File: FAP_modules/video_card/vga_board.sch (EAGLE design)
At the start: 32 parts, among them IC1 IS61LV256, IC2 IS61LV256

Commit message: vga pcb trace fix
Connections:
- net +3V3: now also LED2.A
- net GND: no longer R14.1
- net N$36: now also R14.1; no longer LED2.A
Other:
- moved on the sheet: LED2, R14
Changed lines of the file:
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@@
 <part name="LED2" library="cpu_board" deviceset="LED" device="CHIP-LED0805"/>
 <part name="R14" library="cpu_board" deviceset="RESISTOR" device="0805-RES"/>
-<part name="GND13" library="supply1" deviceset="GND" device=""/>
 <part name="JP1" library="pinhead" deviceset="PINHD-1X1" device=""/>
 <part name="JP2" library="pinhead" deviceset="PINHD-1X1" device=""/>
@@
 <part name="+3V10" library="supply1" deviceset="+3V3" device=""/>
 <part name="+3V11" library="supply1" deviceset="+3V3" device=""/>
+<part name="+3V12" library="supply1" deviceset="+3V3" device=""/>
 </parts>
 <sheets>
@@
 <instance part="GND12" gate="1" x="-566.42" y="-254"/>
 <instance part="+3V7" gate="G$1" x="-566.42" y="-231.14" rot="MR0"/>
-<instance part="LED2" gate="G$1" x="-274.32" y="-137.16"/>
-<instance part="R14" gate="G$1" x="-274.32" y="-147.32" rot="R90"/>
-<instance part="GND13" gate="1" x="-274.32" y="-154.94"/>
+<instance part="LED2" gate="G$1" x="-274.32" y="-114.3"/>
+<instance part="R14" gate="G$1" x="-274.32" y="-127" rot="R90"/>
 <instance part="JP1" gate="G$1" x="-256.54" y="-132.08"/>
 <instance part="JP2" gate="G$1" x="-231.14" y="-132.08"/>
@@
 <instance part="+3V10" gate="G$1" x="-520.7" y="193.04"/>
 <instance part="+3V11" gate="G$1" x="-510.54" y="193.04"/>
+<instance part="+3V12" gate="G$1" x="-274.32" y="-104.14"/>
 </instances>
 <busses>
@@
 </segment>
 <segment>
-<pinref part="R14" gate="G$1" pin="1"/>
-<pinref part="GND13" gate="1" pin="GND"/>
-</segment>
-<segment>
 <pinref part="JP2" gate="G$1" pin="1"/>
 <pinref part="GND14" gate="1" pin="GND"/>
@@
 <pinref part="+3V11" gate="G$1" pin="+3V3"/>
 </segment>
+<segment>
+<pinref part="+3V12" gate="G$1" pin="+3V3"/>
+<pinref part="LED2" gate="G$1" pin="A"/>
+<wire x1="-274.32" y1="-111.76" x2="-274.32" y2="-106.68" width="0.1524" layer="91"/>
+</segment>
 </net>
 <net name="+5V" class="0">
@@
 </segment>
 </net>
-<net name="N$35" class="0">
-<segment>
-<pinref part="LED2" gate="G$1" pin="C"/>
-<pinref part="R14" gate="G$1" pin="2"/>
-</segment>
-</net>
 <net name="N$36" class="0">
 <segment>
@@
 <wire x1="-383.54" y1="-132.08" x2="-370.84" y2="-132.08" width="0.1524" layer="91"/>
 <wire x1="-370.84" y1="-132.08" x2="-274.32" y2="-132.08" width="0.1524" layer="91"/>
-<wire x1="-274.32" y1="-132.08" x2="-274.32" y2="-134.62" width="0.1524" layer="91"/>
-<pinref part="LED2" gate="G$1" pin="A"/>
 <pinref part="JP1" gate="G$1" pin="1"/>
-<wire x1="-259.08" y1="-132.08" x2="-274.32" y2="-132.08" width="0.1524" layer="91"/>
-<junction x="-274.32" y="-132.08"/>
 <pinref part="U$1" gate="G$1" pin="30"/>
+<wire x1="-274.32" y1="-132.08" x2="-259.08" y2="-132.08" width="0.1524" layer="91"/>
 <wire x1="-370.84" y1="-246.38" x2="-370.84" y2="-132.08" width="0.1524" layer="91"/>
 <junction x="-370.84" y="-132.08"/>
+<pinref part="R14" gate="G$1" pin="1"/>
+<junction x="-274.32" y="-132.08"/>
 </segment>
 </net>
@@
 </segment>
 </net>
+<net name="N$35" class="0">
+<segment>
+<pinref part="LED2" gate="G$1" pin="C"/>
+<pinref part="R14" gate="G$1" pin="2"/>
+<wire x1="-274.32" y1="-121.92" x2="-274.32" y2="-119.38" width="0.1524" layer="91"/>
+</segment>
+</net>

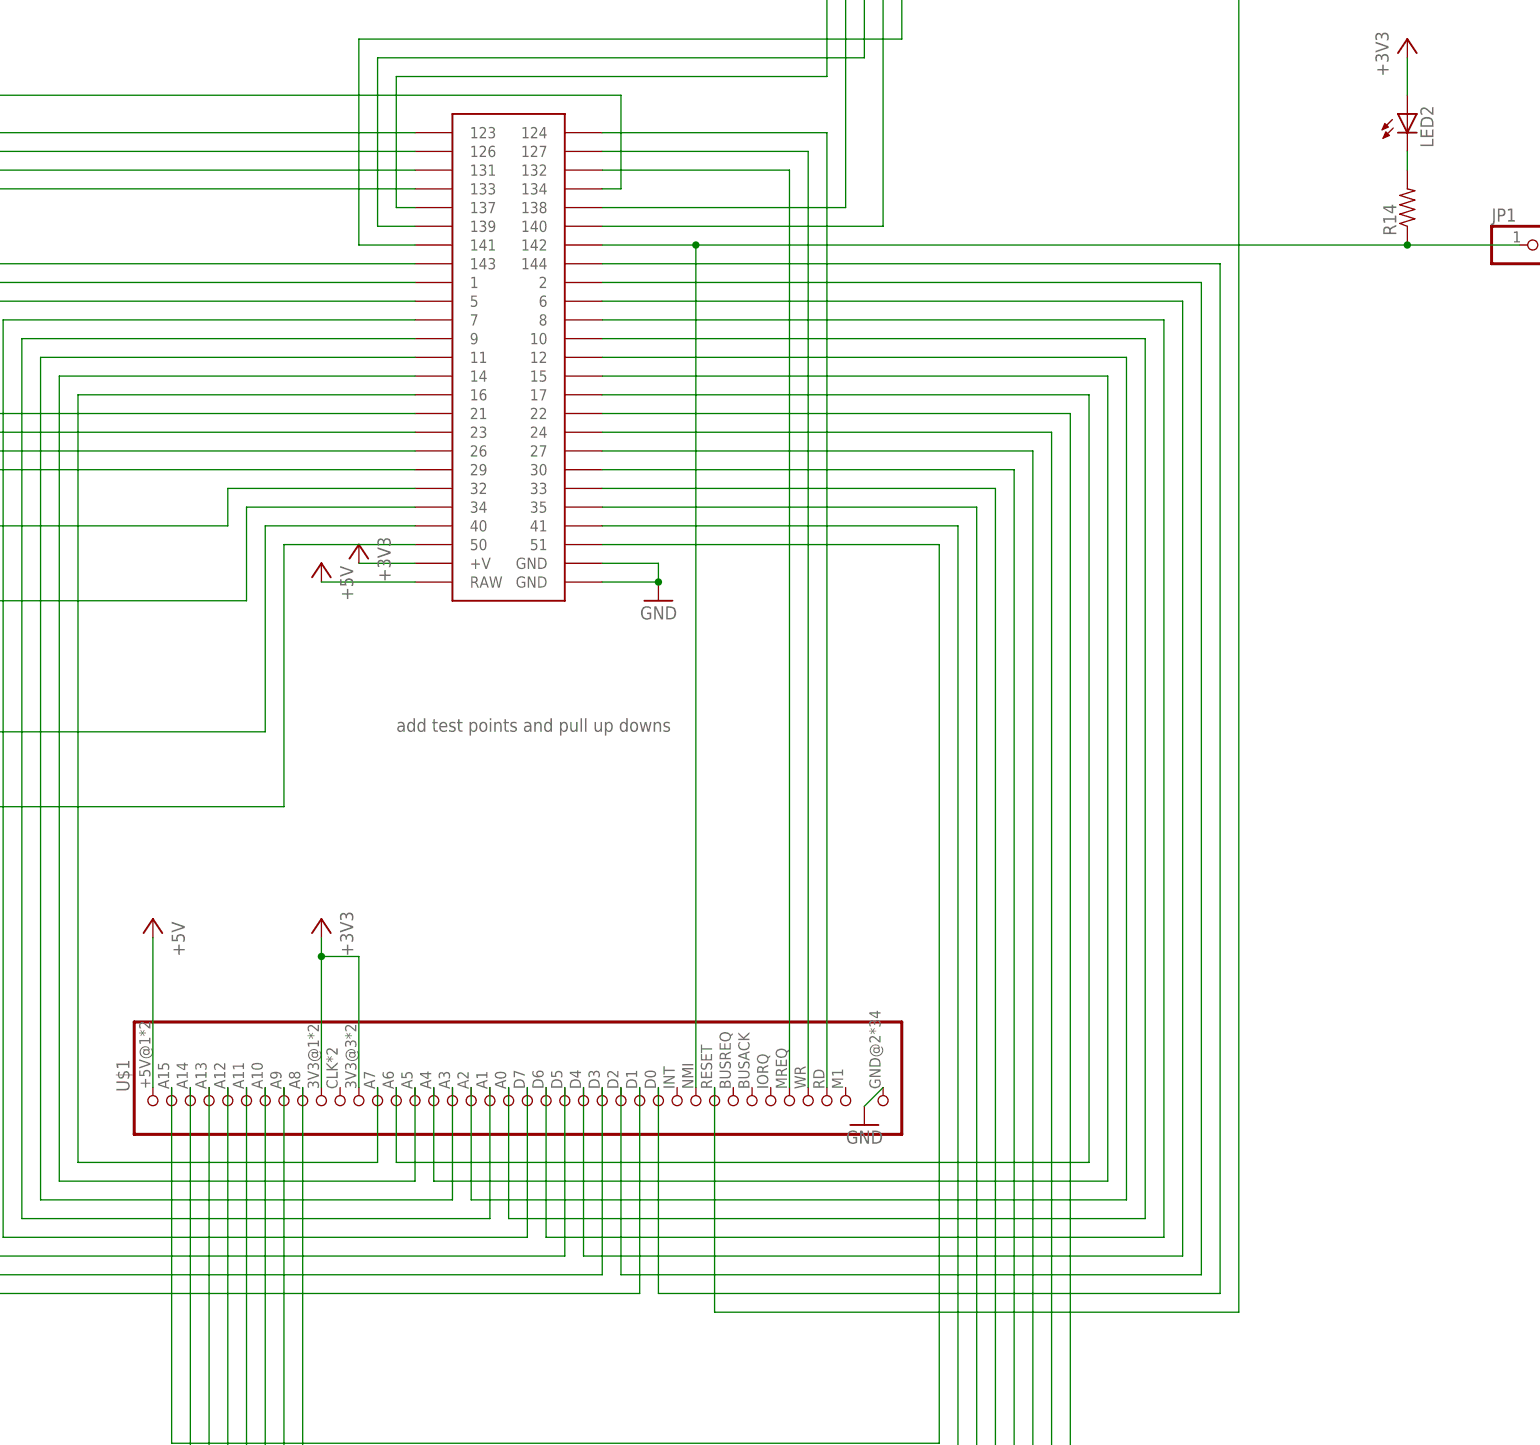
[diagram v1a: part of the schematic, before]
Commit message: added interrupt chaining and WAIT
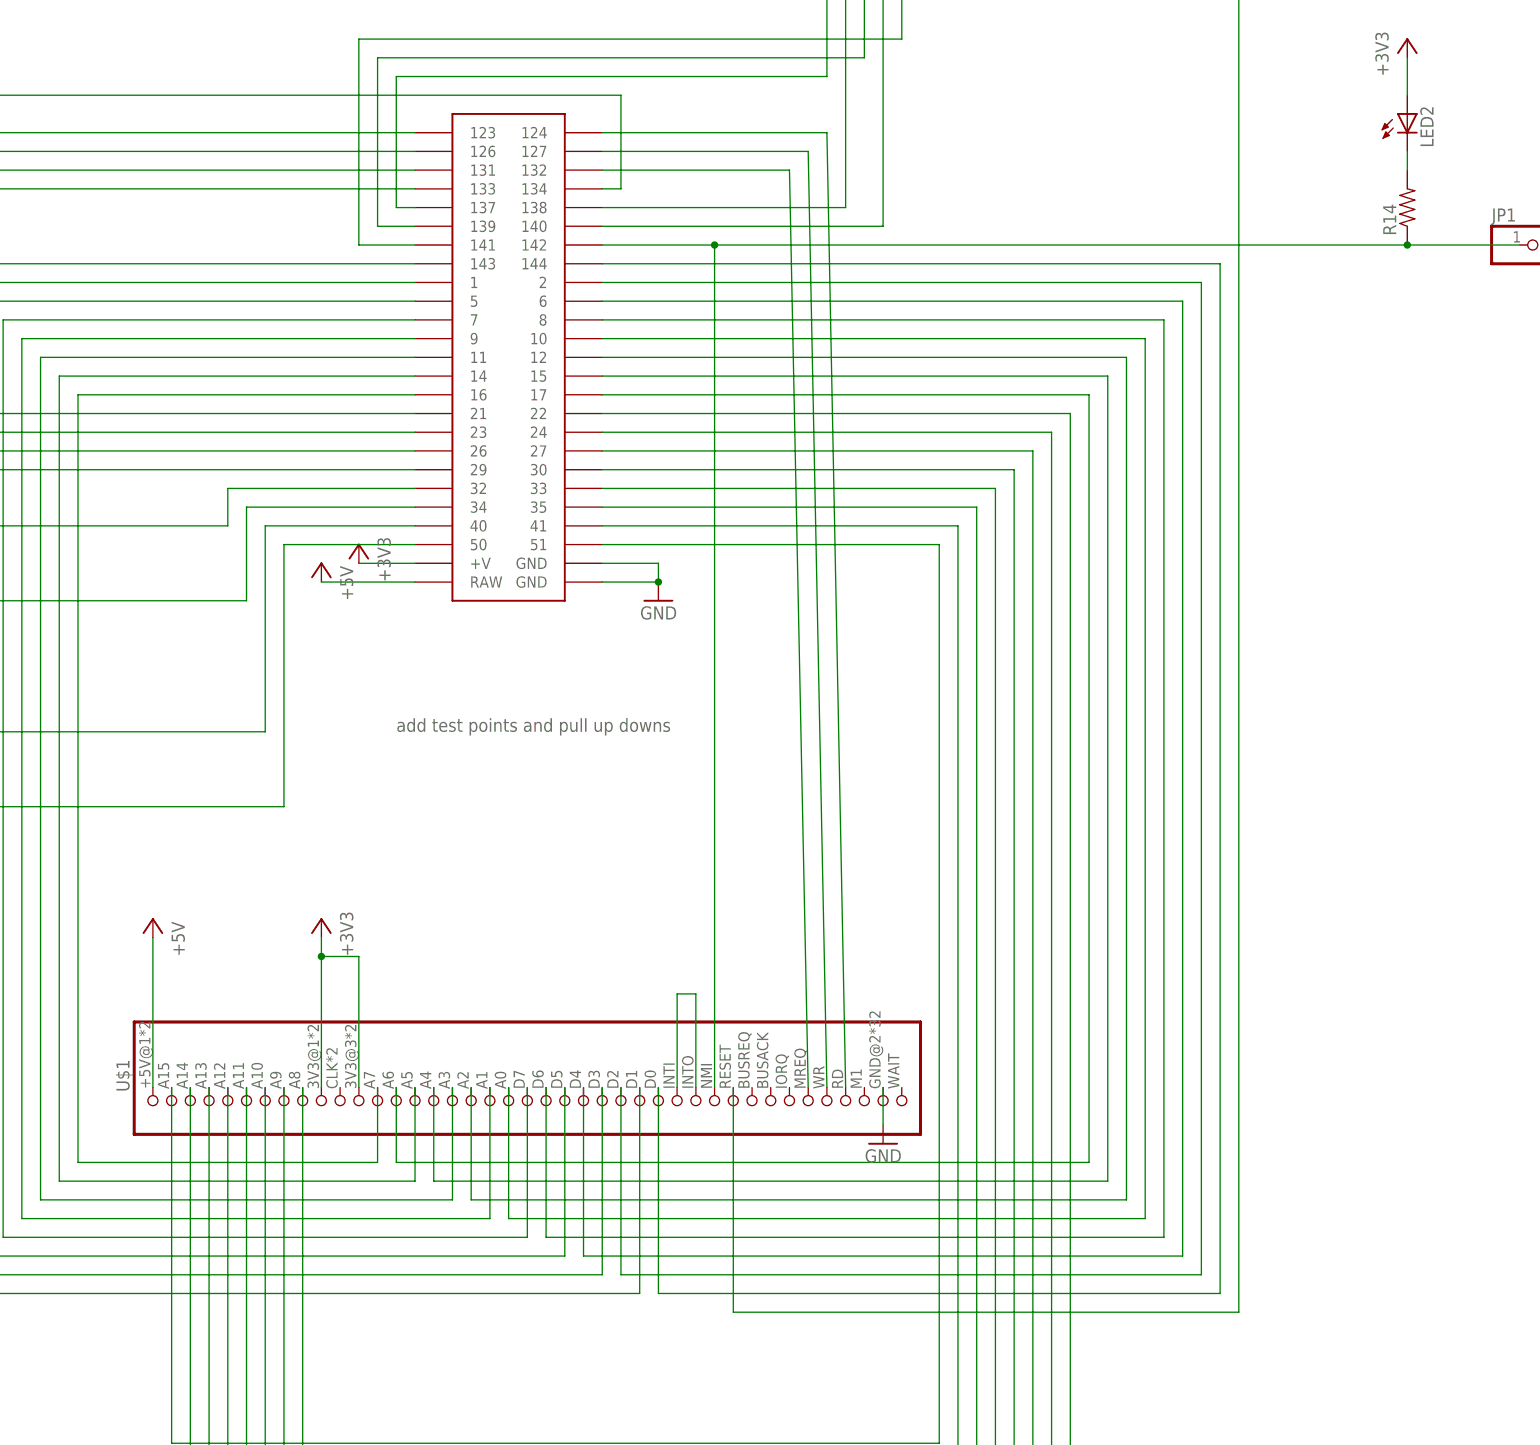
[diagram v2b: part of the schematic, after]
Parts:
- U$1: value FAP_BUS -> FAP_BUS_FAP_BUS; device fap_bus:FAP_BUS -> cpu_board:FAP_BUS_FAP_BUS
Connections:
- new net N$38: U$1.29, U$1.39
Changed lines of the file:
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@@
 <part name="GND3" library="supply1" deviceset="GND" device=""/>
 <part name="GND8" library="supply1" deviceset="GND" device=""/>
-<part name="U$1" library="fap_bus" deviceset="FAP_BUS" device=""/>
+<part name="U$1" library="cpu_board" deviceset="FAP_BUS_FAP_BUS" device=""/>
 <part name="+3V1" library="supply1" deviceset="+3V3" device=""/>
 <part name="P+1" library="supply1" deviceset="+5V" device=""/>
@@
 <instance part="+3V1" gate="G$1" x="-421.64" y="-223.52" rot="MR0"/>
 <instance part="P+1" gate="1" x="-444.5" y="-223.52" rot="MR0"/>
-<instance part="GND4" gate="1" x="-347.98" y="-251.46" rot="MR0"/>
+<instance part="GND4" gate="1" x="-345.44" y="-254" rot="MR0"/>
 <instance part="IC1" gate="G$1" x="-403.86" y="226.06"/>
 <instance part="IC2" gate="G$1" x="-403.86" y="-30.48"/>
@@
 <pinref part="U$1" gate="G$1" pin="GND"/>
 <pinref part="GND4" gate="1" pin="GND"/>
-<wire x1="-347.98" y1="-248.92" x2="-345.44" y2="-246.38" width="0.1524" layer="91"/>
+<wire x1="-345.44" y1="-251.46" x2="-345.44" y2="-246.38" width="0.1524" layer="91"/>
 </segment>
 <segment>
@@
 <pinref part="U$1" gate="G$1" pin="37"/>
 <wire x1="-383.54" y1="-116.84" x2="-353.06" y2="-116.84" width="0.1524" layer="91"/>
-<wire x1="-353.06" y1="-116.84" x2="-353.06" y2="-246.38" width="0.1524" layer="91"/>
+<wire x1="-353.06" y1="-116.84" x2="-350.52" y2="-246.38" width="0.1524" layer="91"/>
 </segment>
 </net>
@@
 <pinref part="U$1" gate="G$1" pin="36"/>
 <wire x1="-383.54" y1="-119.38" x2="-355.6" y2="-119.38" width="0.1524" layer="91"/>
-<wire x1="-355.6" y1="-119.38" x2="-355.6" y2="-246.38" width="0.1524" layer="91"/>
+<wire x1="-355.6" y1="-119.38" x2="-353.06" y2="-246.38" width="0.1524" layer="91"/>
 </segment>
 </net>
@@
 <segment>
 <pinref part="U$1" gate="G$1" pin="35"/>
-<wire x1="-358.14" y1="-246.38" x2="-358.14" y2="-121.92" width="0.1524" layer="91"/>
+<wire x1="-355.6" y1="-246.38" x2="-358.14" y2="-121.92" width="0.1524" layer="91"/>
 <pinref part="U$3" gate="G$2" pin="132"/>
 <wire x1="-358.14" y1="-121.92" x2="-383.54" y2="-121.92" width="0.1524" layer="91"/>
@@
 <segment>
 <pinref part="U$3" gate="G$2" pin="142"/>
-<wire x1="-383.54" y1="-132.08" x2="-370.84" y2="-132.08" width="0.1524" layer="91"/>
-<wire x1="-370.84" y1="-132.08" x2="-274.32" y2="-132.08" width="0.1524" layer="91"/>
+<wire x1="-383.54" y1="-132.08" x2="-368.3" y2="-132.08" width="0.1524" layer="91"/>
+<wire x1="-368.3" y1="-132.08" x2="-274.32" y2="-132.08" width="0.1524" layer="91"/>
 <pinref part="JP1" gate="G$1" pin="1"/>
 <pinref part="U$1" gate="G$1" pin="30"/>
 <wire x1="-274.32" y1="-132.08" x2="-259.08" y2="-132.08" width="0.1524" layer="91"/>
-<wire x1="-370.84" y1="-246.38" x2="-370.84" y2="-132.08" width="0.1524" layer="91"/>
-<junction x="-370.84" y="-132.08"/>
+<wire x1="-368.3" y1="-246.38" x2="-368.3" y2="-132.08" width="0.1524" layer="91"/>
+<junction x="-368.3" y="-132.08"/>
 <pinref part="R14" gate="G$1" pin="1"/>
 <junction x="-274.32" y="-132.08"/>
@@
 <wire x1="-297.18" y1="45.72" x2="-297.18" y2="-276.86" width="0.1524" layer="91"/>
 <pinref part="U$1" gate="G$1" pin="31"/>
-<wire x1="-297.18" y1="-276.86" x2="-368.3" y2="-276.86" width="0.1524" layer="91"/>
-<wire x1="-368.3" y1="-276.86" x2="-368.3" y2="-246.38" width="0.1524" layer="91"/>
+<wire x1="-297.18" y1="-276.86" x2="-365.76" y2="-276.86" width="0.1524" layer="91"/>
+<wire x1="-365.76" y1="-276.86" x2="-365.76" y2="-246.38" width="0.1524" layer="91"/>
 </segment>
 </net>
@@
 </segment>
 </net>
+<net name="N$38" class="0">
+<segment>
+<pinref part="U$1" gate="G$1" pin="29"/>
+<wire x1="-373.38" y1="-246.38" x2="-373.38" y2="-233.68" width="0.1524" layer="91"/>
+<pinref part="U$1" gate="G$1" pin="39"/>
+<wire x1="-373.38" y1="-233.68" x2="-370.84" y2="-233.68" width="0.1524" layer="91"/>
+<wire x1="-370.84" y1="-233.68" x2="-370.84" y2="-246.38" width="0.1524" layer="91"/>
+</segment>
+</net>

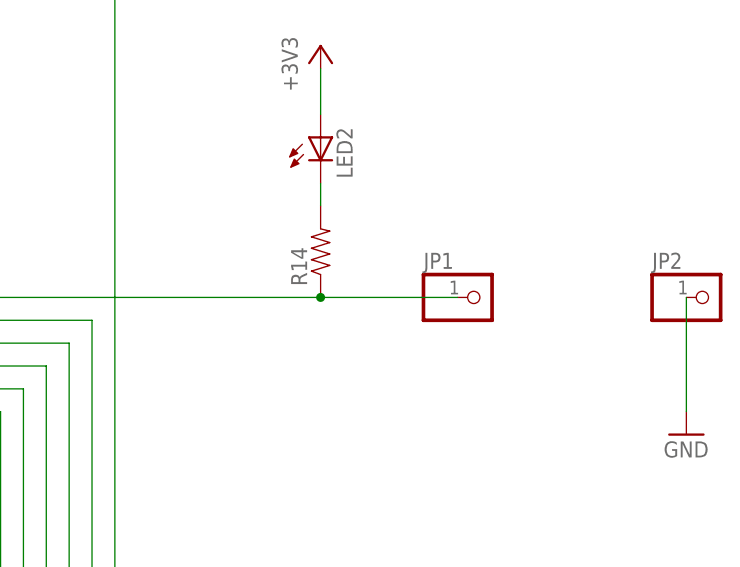
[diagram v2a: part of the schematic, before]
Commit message: moved VGA sockect
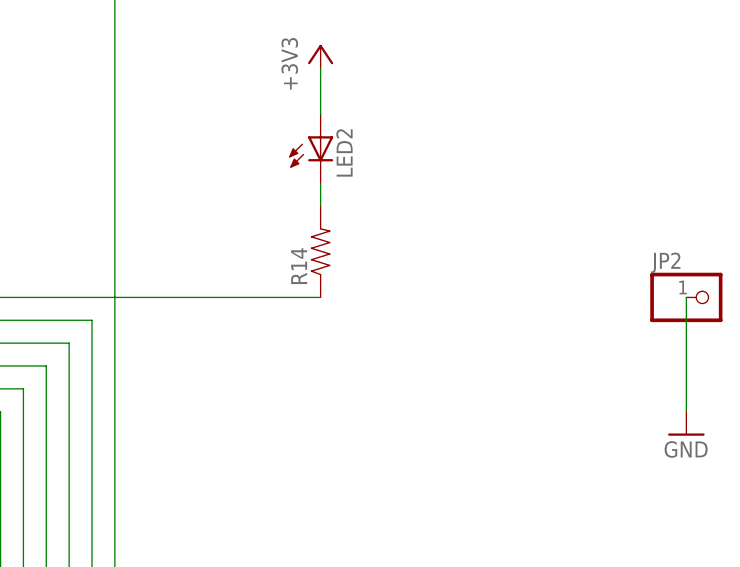
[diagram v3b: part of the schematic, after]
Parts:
- removed JP1: (no value), pinhead:PINHD-1X1
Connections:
- net N$36: no longer JP1.1
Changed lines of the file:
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@@
 <part name="LED2" library="cpu_board" deviceset="LED" device="CHIP-LED0805"/>
 <part name="R14" library="cpu_board" deviceset="RESISTOR" device="0805-RES"/>
-<part name="JP1" library="pinhead" deviceset="PINHD-1X1" device=""/>
 <part name="JP2" library="pinhead" deviceset="PINHD-1X1" device=""/>
 <part name="GND14" library="supply1" deviceset="GND" device=""/>
@@
 <instance part="LED2" gate="G$1" x="-274.32" y="-114.3"/>
 <instance part="R14" gate="G$1" x="-274.32" y="-127" rot="R90"/>
-<instance part="JP1" gate="G$1" x="-256.54" y="-132.08"/>
 <instance part="JP2" gate="G$1" x="-231.14" y="-132.08"/>
 <instance part="GND14" gate="1" x="-233.68" y="-147.32"/>
@@
 <wire x1="-383.54" y1="-132.08" x2="-368.3" y2="-132.08" width="0.1524" layer="91"/>
 <wire x1="-368.3" y1="-132.08" x2="-274.32" y2="-132.08" width="0.1524" layer="91"/>
-<pinref part="JP1" gate="G$1" pin="1"/>
 <pinref part="U$1" gate="G$1" pin="30"/>
-<wire x1="-274.32" y1="-132.08" x2="-259.08" y2="-132.08" width="0.1524" layer="91"/>
 <wire x1="-368.3" y1="-246.38" x2="-368.3" y2="-132.08" width="0.1524" layer="91"/>
 <junction x="-368.3" y="-132.08"/>
 <pinref part="R14" gate="G$1" pin="1"/>
-<junction x="-274.32" y="-132.08"/>
-</segment>
-</net>
+</segment>
+</net>
